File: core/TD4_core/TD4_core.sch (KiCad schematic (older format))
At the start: 7 parts, among them J1 Conn_02x32_Row_Letter_First

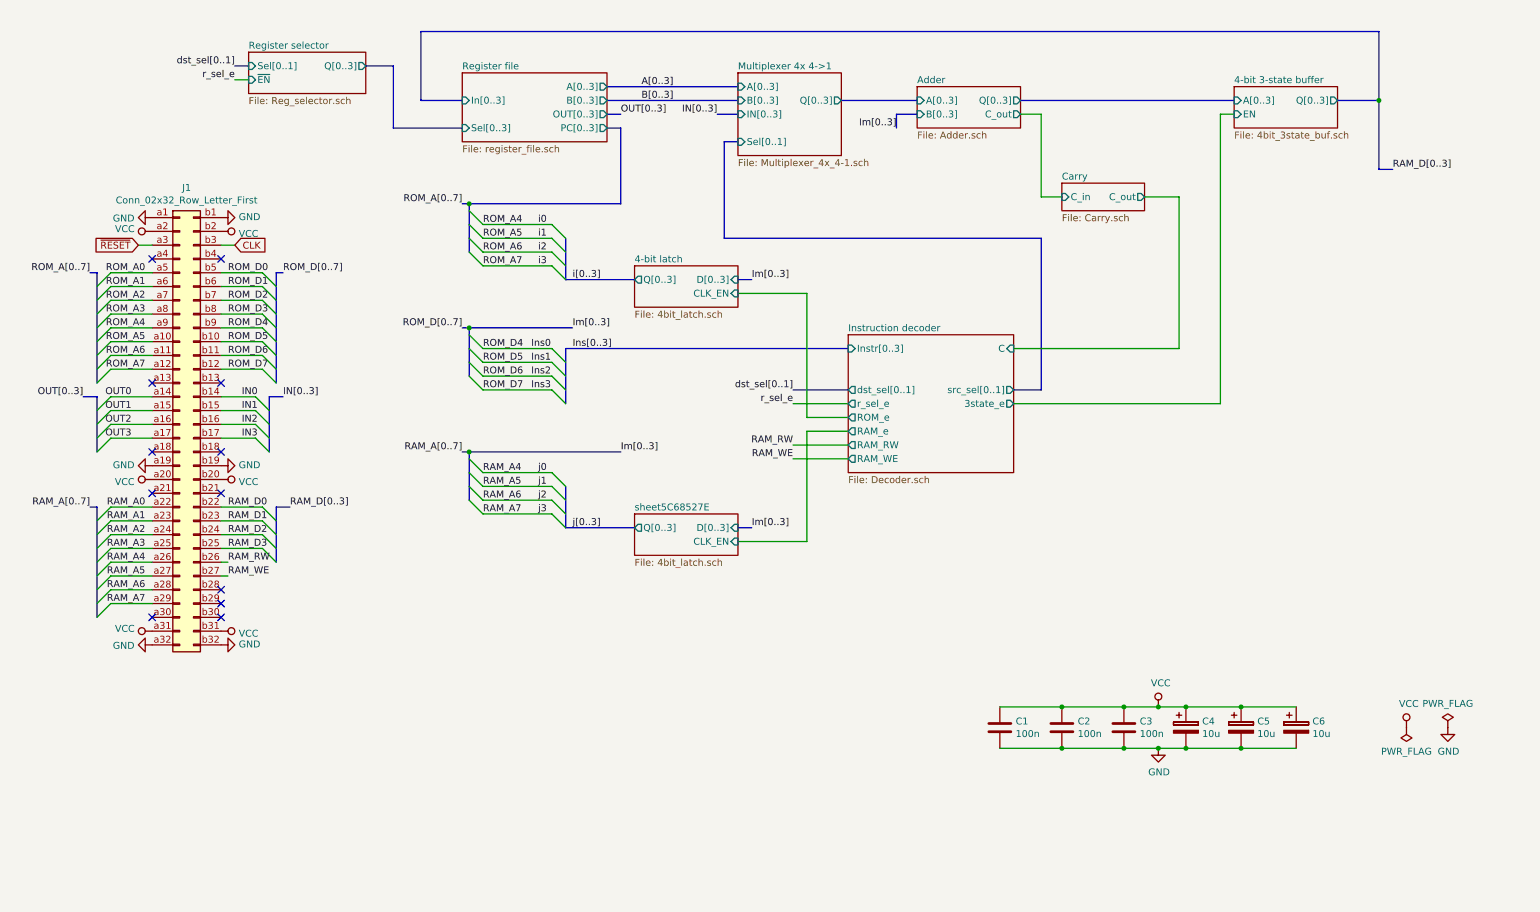
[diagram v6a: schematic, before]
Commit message: Added debug headers to core
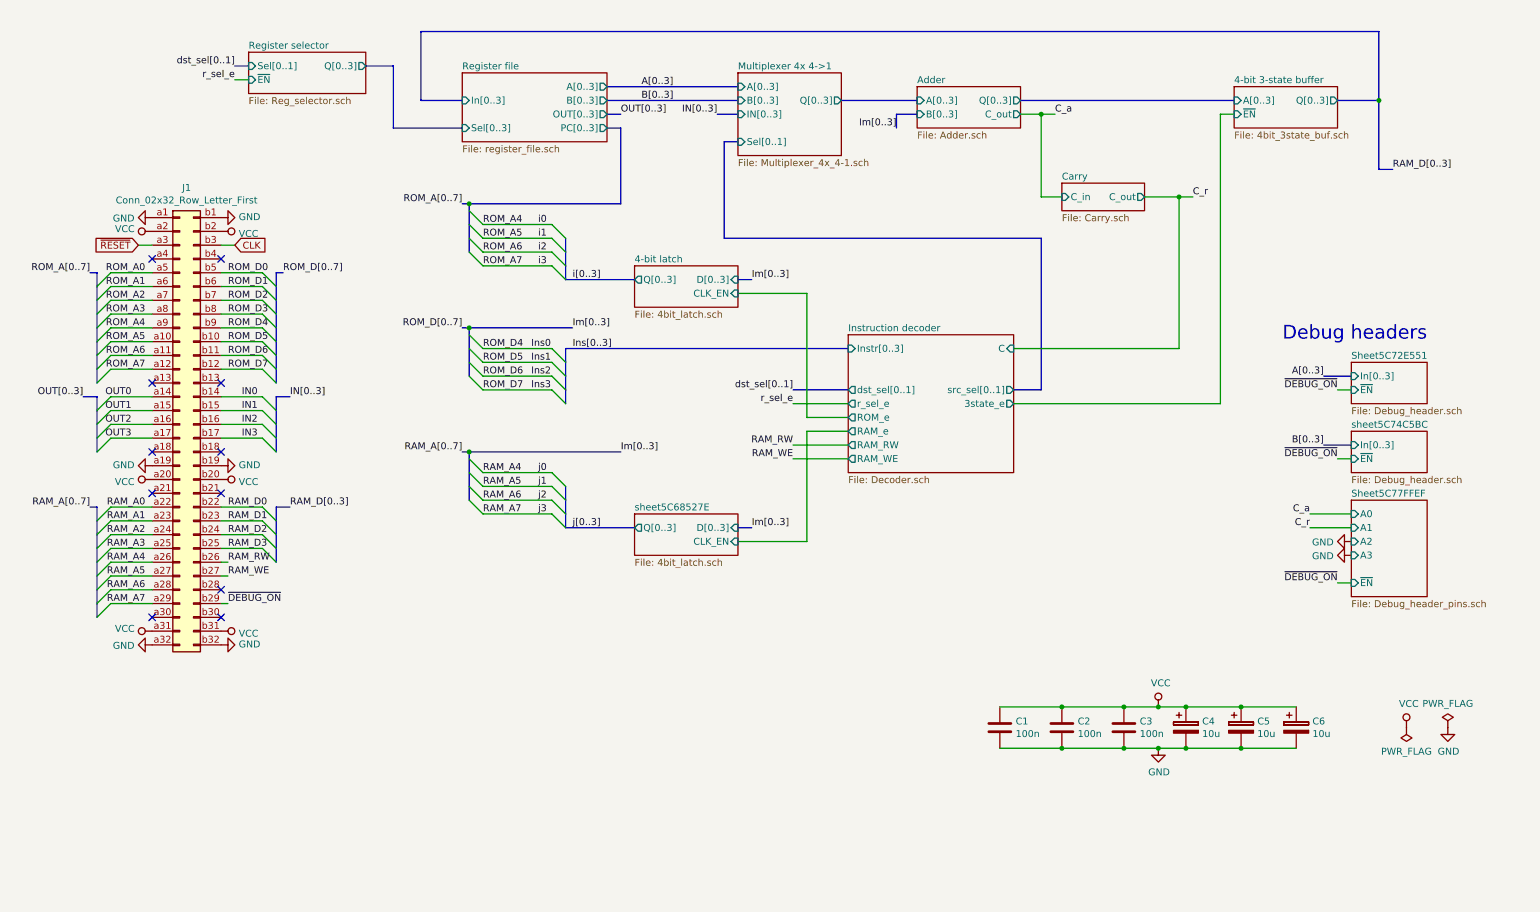
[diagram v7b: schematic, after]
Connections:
- net ~DEBUG_ON~: now reaches J1.b29 (Pin_b29)
- no-connect marks 12 -> 11
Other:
- note added: "Debug headers"
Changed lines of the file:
@@
 $Descr A4 11693 8268
 encoding utf-8
-Sheet 1 23
+Sheet 1 30
 Title "TD4 core module"
 Date ""
@@
 F2 "Q[0..3]" O R 10050 1600 50
 F3 "A[0..3]" I L 9300 1600 50
-F4 "EN" I L 9300 1700 50
+F4 "~EN" I L 9300 1700 50
 $EndSheet
 Wire Bus Line
@@
 Im[0..3]
 Entry Wire Line
-	2200 3750 2300 3850
-Entry Wire Line
-	2200 3850 2300 3950
-Entry Wire Line
-	2200 3950 2300 4050
-Entry Wire Line
-	2200 4050 2300 4150
+	2250 3750 2350 3850
+Entry Wire Line
+	2250 3850 2350 3950
+Entry Wire Line
+	2250 3950 2350 4050
+Entry Wire Line
+	2250 4050 2350 4150
 Entry Wire Line
 	1150 3750 1050 3850
@@
 OUT3
 Wire Bus Line
-	2300 3750 2400 3750
+	2350 3750 2450 3750
 Wire Bus Line
 	1050 3750 950  3750
-Text Label 2400 3750 0    50   ~ 0
+Text Label 2450 3750 0    50   ~ 0
 IN[0..3]
 Text Label 950  3750 2    50   ~ 0
@@
 	1150 3850 1450 3850
 Wire Wire Line
-	1950 3750 2200 3750
+	1950 3750 2250 3750
 Wire Bus Line
 	3700 4150 3750 4150
 Wire Wire Line
-	1950 3850 2200 3850
-Wire Wire Line
-	1950 3950 2200 3950
-Wire Wire Line
-	1950 4050 2200 4050
+	1950 3850 2250 3850
+Wire Wire Line
+	1950 3950 2250 3950
+Wire Wire Line
+	1950 4050 2250 4050
 Connection ~ 3750 4150
 Wire Bus Line
@@
 $EndComp
 NoConn ~ 1950 5150
-NoConn ~ 1950 5250
 $Comp
 L Device:CP C6
@@
 Wire Wire Line
 	8750 6300 8950 6300
+Wire Wire Line
+	1950 5250 2000 5250
+Text Label 2000 5250 0    50   ~ 0
+~DEBUG_ON~
+Wire Wire Line
+	10050 3700 10150 3700
+Text Label 10050 3700 2    50   ~ 0
+~DEBUG_ON~
+Wire Bus Line
+	9950 3600 10150 3600
+Text Notes 9650 3350 0    100  ~ 0
+Debug headers
+Text Label 9950 3600 2    50   ~ 0
+A[0..3]
+$Sheet
+S 10150 3500 550  300
+U 5C72E552
+F0 "Sheet5C72E551" 50
+F1 "Debug_header.sch" 50
+F2 "In[0..3]" I L 10150 3600 50
+F3 "~EN" I L 10150 3700 50
+$EndSheet
+Wire Wire Line
+	10050 4200 10150 4200
+Text Label 10050 4200 2    50   ~ 0
+~DEBUG_ON~
+Wire Bus Line
+	9950 4100 10150 4100
+Text Label 9950 4100 2    50   ~ 0
+B[0..3]
+$Sheet
+S 10150 4000 550  300
+U 5C74C5C4
+F0 "sheet5C74C5BC" 50
+F1 "Debug_header.sch" 50
+F2 "In[0..3]" I L 10150 4100 50
+F3 "~EN" I L 10150 4200 50
+$EndSheet
+$Sheet
+S 10150 4500 550  700
+U 5C77FFF0
+F0 "Sheet5C77FFEF" 50
+F1 "Debug_header_pins.sch" 50
+F2 "~EN" I L 10150 5100 50
+F3 "A0" I L 10150 4600 50
+F4 "A1" I L 10150 4700 50
+F5 "A2" I L 10150 4800 50
+F6 "A3" I L 10150 4900 50
+$EndSheet
+Wire Wire Line
+	10050 5100 10150 5100
+Text Label 10050 5100 2    50   ~ 0
+~DEBUG_ON~
+$Comp
+L power:GND #PWR?
+U 1 1 5C78D936
+P 10150 4900
+F 0 "#PWR?" H 10150 4650 50  0001 C CNN
+F 1 "GND" V 10155 4772 50  0000 R CNN
+F 2 "" H 10150 4900 50  0001 C CNN
+F 3 "" H 10150 4900 50  0001 C CNN
+	1    10150 4900
+	0    1    1    0
+$EndComp
+Wire Wire Line
+	10150 4600 9850 4600
+Wire Wire Line
+	7900 1700 8000 1700
+Connection ~ 7900 1700
+Wire Wire Line
+	8900 2300 9000 2300
+Connection ~ 8900 2300
+Text Label 8000 1700 0    50   ~ 0
+C_a
+Text Label 9000 2300 0    50   ~ 0
+C_r
+Wire Wire Line
+	10150 4700 9850 4700
+Text Label 9850 4600 2    50   ~ 0
+C_a
+Text Label 9850 4700 2    50   ~ 0
+C_r
+$Comp
+L power:GND #PWR?
+U 1 1 5C7B1C3E
+P 10150 4800
+F 0 "#PWR?" H 10150 4550 50  0001 C CNN
+F 1 "GND" V 10155 4672 50  0000 R CNN
+F 2 "" H 10150 4800 50  0001 C CNN
+F 3 "" H 10150 4800 50  0001 C CNN
+	1    10150 4800
+	0    1    1    0
+$EndComp
 Wire Bus Line
 	4450 2600 4450 2900
@@
 	1050 3750 1050 4150
 Wire Bus Line
-	2300 3750 2300 4150
+	2350 3750 2350 4150
 Wire Bus Line
 	3750 2350 3750 2700
